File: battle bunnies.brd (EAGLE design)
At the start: 151.7 x 94 mm, 59 parts, among them IC1 CP2104, Q1 mmbt2222, Q2 mmbt2222, SW2 KMR2, U1 PCA9685, U2 SPX3819, U3 MCP73831T-2ACI/OT, X2 ESP-12, X4 20329

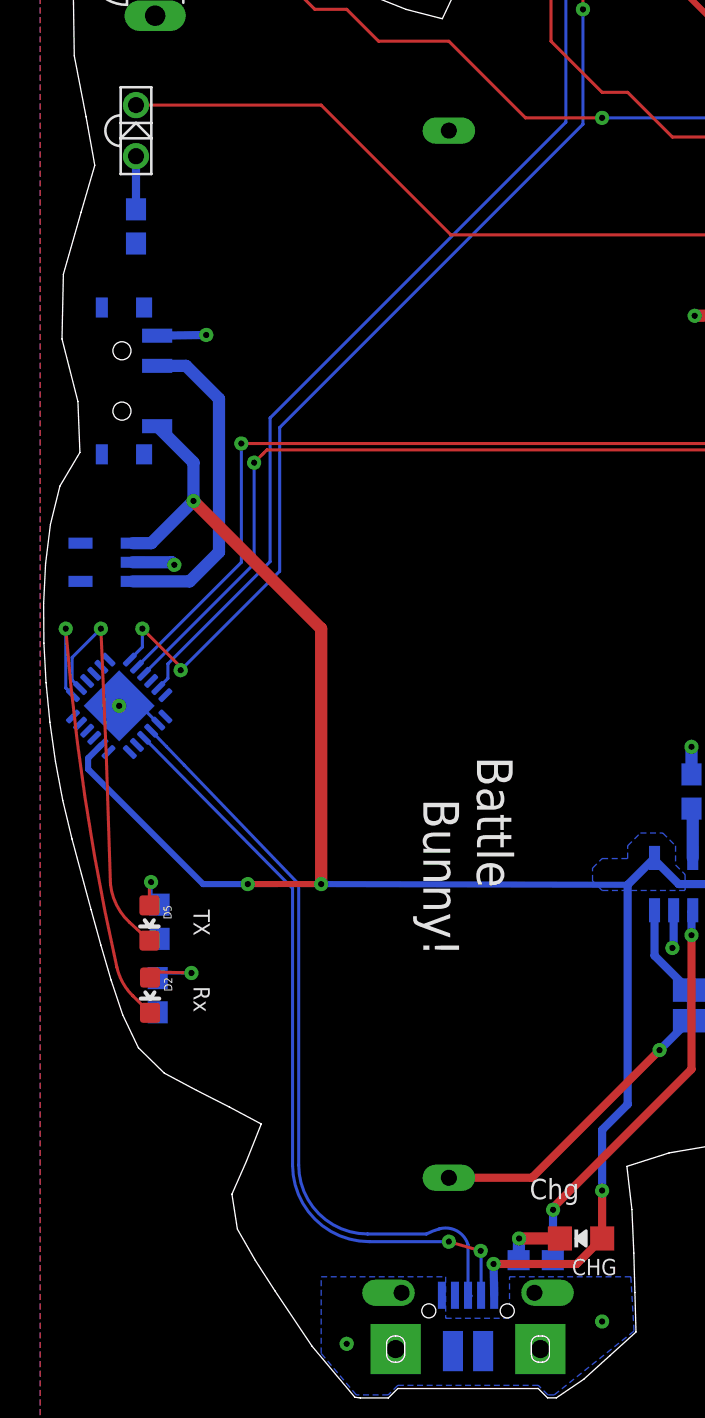
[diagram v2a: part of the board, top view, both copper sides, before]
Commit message: Fixing the USB impedance issue (moving USB chip)
This is a pretty big change as I'm moving a bunch of stuff around
which obviously causes it's own issues, but this should be ok
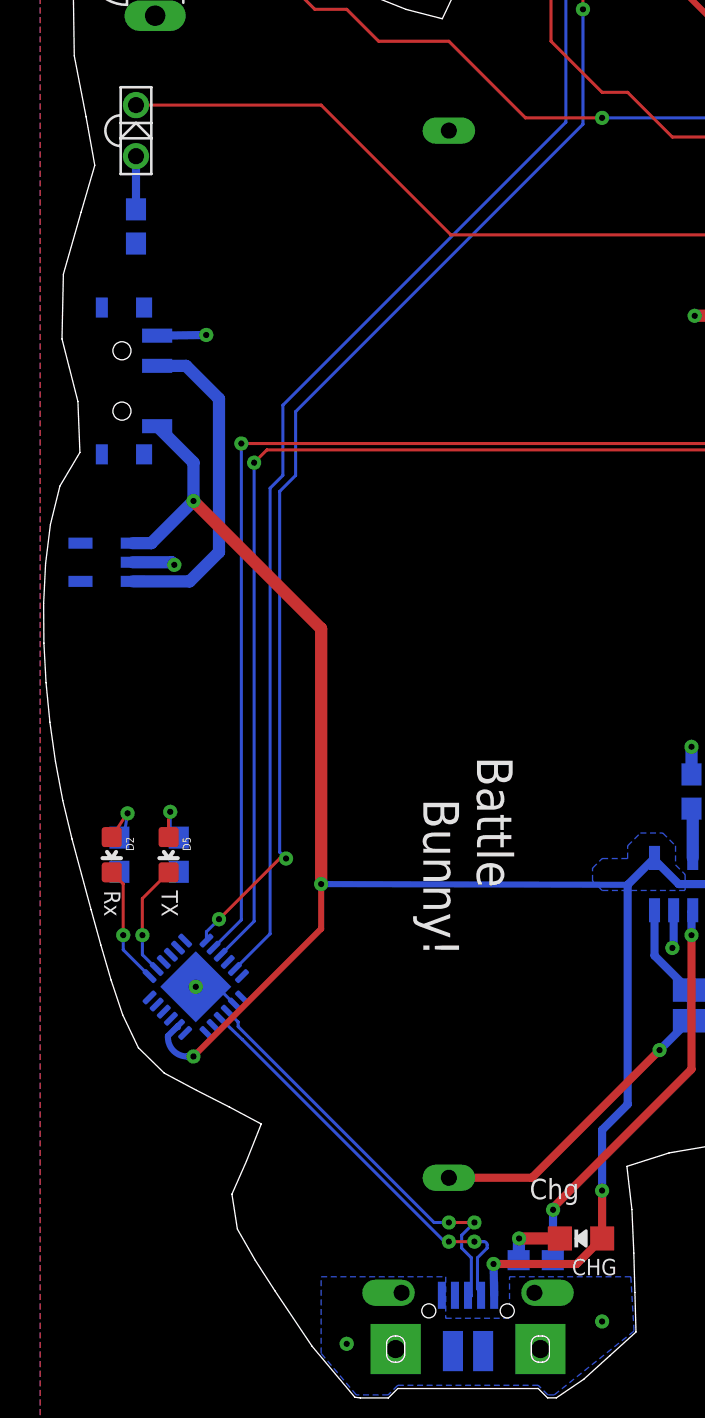
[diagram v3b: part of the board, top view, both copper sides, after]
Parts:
- moved IC1 14.5 mm to (7.74, 21.6)
- moved D2 7.24 mm to (3.56, 28.1)
- moved R15 7.24 mm to (3.94, 28.1)
- moved D5 3.53 mm to (6.38, 28.1)
- moved R1 3.47 mm to (6.89, 28.1)
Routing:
- net RXLED: track 23.3 -> 5.94 mm
- net USBD_N: track 37.5 -> 20.6 mm
- net USBD_P: track 37.3 -> 21.0 mm, vias 0 -> 2
- net TXLED: track 19.9 -> 5.64 mm
- net DTR: track 49.3 -> 61.7 mm
- net USB_RX: track 51.0 -> 63.4 mm
- net TXD: track 177.3 -> 189.7 mm
- net RTS: track 52.7 -> 61.5 mm
- net VBUS: track 98.2 -> 96.4 mm
- net N$10: track 3.96 -> 2.74 mm

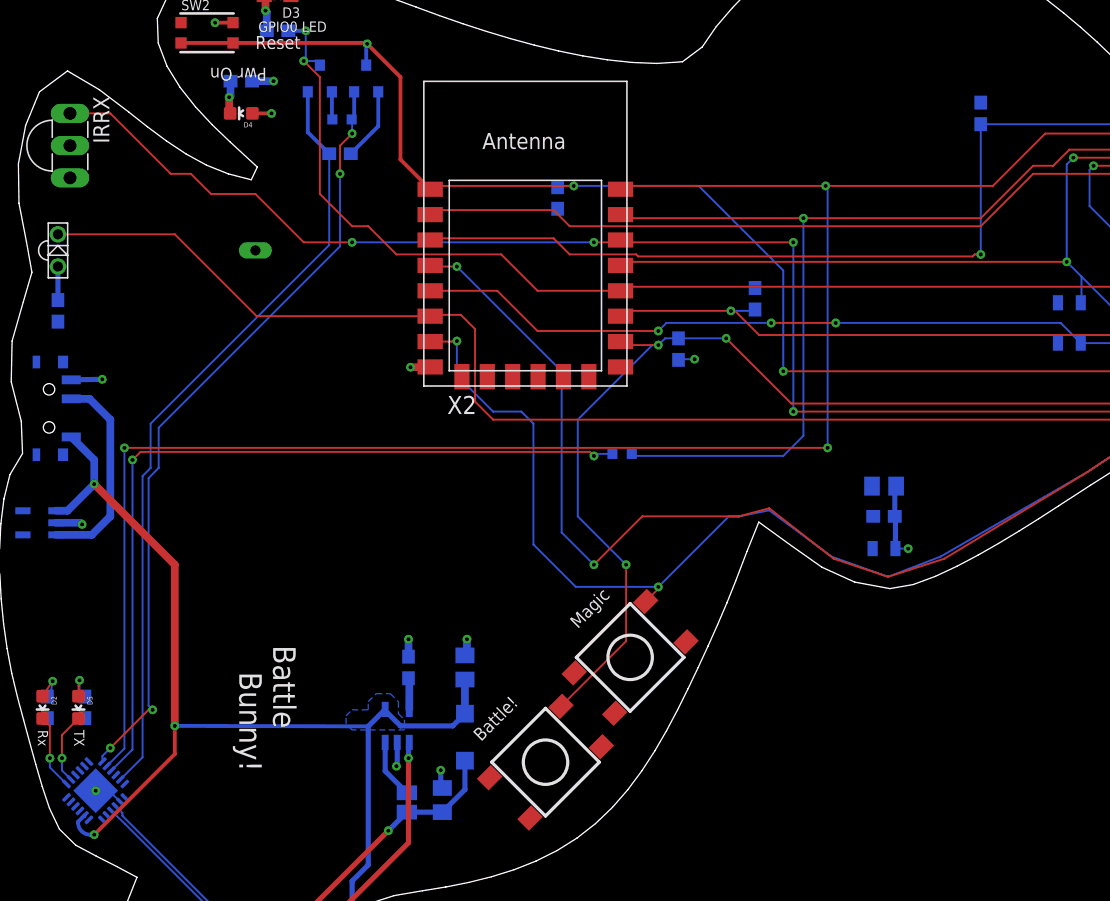
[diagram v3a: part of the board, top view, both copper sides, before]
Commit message: Adding some clearances around lines passing through the ESP8266
This *SHOULDN'T* be the problem with the IR RX but it can't hurt
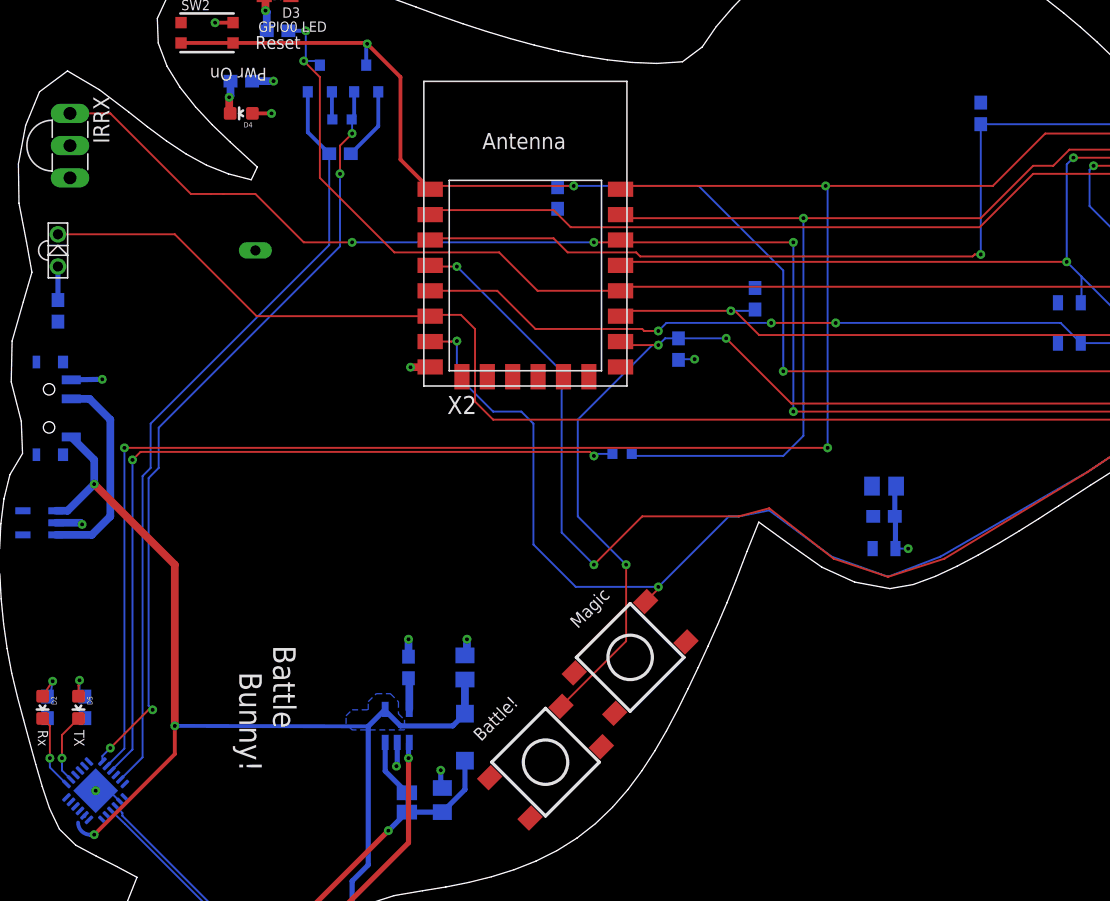
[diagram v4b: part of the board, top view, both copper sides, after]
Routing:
- net VBUS: track 96.4 -> 95.7 mm
- net GPIO0: track 147.4 -> 146.6 mm
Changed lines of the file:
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@@
 <wire x1="6.35" y1="19.05" x2="7.3025" y2="18.0975" width="0.3048" layer="16" curve="90"/>
 <wire x1="7.3025" y1="18.0975" x2="7.62" y2="18.0975" width="0.3048" layer="16"/>
-<wire x1="6.35" y1="19.05" x2="6.35" y2="19.117696875" width="0.3048" layer="16"/>
-<wire x1="6.35" y1="19.117696875" x2="6.8518375" y2="19.619534375" width="0.3048" layer="16"/>
+<wire x1="6.35" y1="19.05" x2="6.8518375" y2="19.5518375" width="0" layer="19" extent="16-16"/>
 </signal>
 <signal name="VBAT">
@@
 <contactref element="JP4" pad="5"/>
 <wire x1="135.5725" y1="87.3125" x2="135.5725" y2="85.725" width="0.1524" layer="1"/>
-<wire x1="81.5975" y1="70.1675" x2="77.47" y2="66.04" width="0.1524" layer="1"/>
-<wire x1="77.47" y1="66.04" x2="45.085" y2="66.04" width="0.1524" layer="1"/>
-<wire x1="45.085" y1="66.04" x2="43.815" y2="67.31" width="0.1524" layer="1"/>
+<wire x1="81.5975" y1="70.1675" x2="77.390625" y2="65.960625" width="0.1524" layer="1"/>
 <wire x1="43.815" y1="67.31" x2="34.45" y2="67.31" width="0.1524" layer="1"/>
 <wire x1="34.45" y1="67.31" x2="34.0925" y2="66.9525" width="0.1524" layer="1"/>
@@
 <wire x1="106.9975" y1="70.1675" x2="81.5975" y2="70.1675" width="0.1524" layer="1"/>
 <wire x1="107.95" y1="71.12" x2="106.9975" y2="70.1675" width="0.1524" layer="1"/>
+<wire x1="43.815" y1="67.31" x2="45.164375" y2="65.960625" width="0.1524" layer="1"/>
+<wire x1="45.164375" y1="65.960625" x2="77.390625" y2="65.960625" width="0.1524" layer="1"/>
 </signal>
 <signal name="CH_PD">
@@
 <contactref element="R3" pad="1"/>
 <contactref element="JP4" pad="10"/>
-<wire x1="45.085" y1="63.8175" x2="43.815" y2="65.0875" width="0.1524" layer="1"/>
 <wire x1="43.815" y1="65.0875" x2="34.2275" y2="65.0875" width="0.1524" layer="1"/>
 <wire x1="34.2275" y1="65.0875" x2="34.0925" y2="64.9525" width="0.1524" layer="1"/>
-<wire x1="45.085" y1="63.8175" x2="50.32375" y2="63.8175" width="0.1524" layer="1"/>
-<wire x1="50.32375" y1="63.8175" x2="50.4825" y2="63.65875" width="0.1524" layer="1"/>
-<wire x1="50.4825" y1="63.65875" x2="76.835" y2="63.65875" width="0.1524" layer="1"/>
+<wire x1="50.64125" y1="63.65875" x2="76.835" y2="63.65875" width="0.1524" layer="1"/>
 <wire x1="76.835" y1="63.65875" x2="76.99375" y2="63.8175" width="0.1524" layer="1"/>
 <wire x1="76.99375" y1="63.8175" x2="77.47" y2="63.8175" width="0.1524" layer="1"/>
@@
 <wire x1="121.76125" y1="80.16875" x2="122.8725" y2="81.28" width="0.1524" layer="16"/>
 <wire x1="122.8725" y1="81.28" x2="122.8725" y2="87.3125" width="0.1524" layer="16"/>
+<wire x1="43.815" y1="65.0875" x2="44.92625" y2="63.97625" width="0.1524" layer="1"/>
+<wire x1="44.92625" y1="63.97625" x2="50.32375" y2="63.97625" width="0.1524" layer="1"/>
+<wire x1="50.32375" y1="63.97625" x2="50.64125" y2="63.65875" width="0.1524" layer="1"/>
 </signal>
 <signal name="GPIO16">
@@
 <contactref element="JP2" pad="3"/>
 <wire x1="49.0925" y1="60.9525" x2="42.5525" y2="60.9525" width="0.1524" layer="1"/>
-<wire x1="42.5525" y1="60.9525" x2="39.6875" y2="63.8175" width="0.1524" layer="1"/>
-<wire x1="39.6875" y1="63.8175" x2="31.4325" y2="63.8175" width="0.1524" layer="1"/>
-<wire x1="31.4325" y1="63.8175" x2="29.21" y2="66.04" width="0.1524" layer="1"/>
-<wire x1="29.21" y1="66.04" x2="27.94" y2="66.04" width="0.1524" layer="1"/>
-<wire x1="27.94" y1="66.04" x2="25.4" y2="68.58" width="0.1524" layer="1"/>
-<wire x1="25.4" y1="68.58" x2="25.4" y2="77.7875" width="0.1524" layer="1"/>
+<wire x1="42.5525" y1="60.9525" x2="39.52875" y2="63.97625" width="0.1524" layer="1"/>
+<wire x1="25.4" y1="69.85" x2="25.4" y2="77.7875" width="0.1524" layer="1"/>
 <wire x1="25.4" y1="77.7875" x2="24.13" y2="79.0575" width="0.1524" layer="1"/>
 <via x="24.13" y="79.0575" extent="1-16" drill="0.3048" diameter="0.3048"/>
@@
 <wire x1="24.28875" y1="81.43875" x2="24.28875" y2="79.21625" width="0.1524" layer="16"/>
 <wire x1="24.28875" y1="79.21625" x2="24.13" y2="79.0575" width="0.1524" layer="16"/>
+<wire x1="39.52875" y1="63.97625" x2="31.27375" y2="63.97625" width="0.1524" layer="1"/>
+<wire x1="31.27375" y1="63.97625" x2="25.4" y2="69.85" width="0.1524" layer="1"/>
 </signal>
 <signal name="RXD">
@@
 <via x="62.70625" y="51.435" extent="1-16" drill="0.3048"/>
 <wire x1="8.89" y1="74.93" x2="5.715" y2="74.93" width="0.1524" layer="1"/>
-<wire x1="16.8275" y1="68.58" x2="15.24" y2="70.1675" width="0.1524" layer="1"/>
-<wire x1="13.6525" y1="70.1675" x2="8.89" y2="74.93" width="0.1524" layer="1"/>
-<wire x1="16.8275" y1="68.58" x2="20.32" y2="68.58" width="0.1524" layer="1"/>
+<wire x1="15.24" y1="68.58" x2="8.89" y2="74.93" width="0.1524" layer="1"/>
+<wire x1="16.8275" y1="68.58" x2="17.78" y2="68.58" width="0.1524" layer="1"/>
+<wire x1="17.78" y1="68.58" x2="20.32" y2="68.58" width="0.1524" layer="1"/>
 <wire x1="20.32" y1="68.58" x2="24.13" y2="64.77" width="0.1524" layer="1"/>
 <wire x1="49.0925" y1="64.9525" x2="48.91" y2="64.77" width="0.1524" layer="1"/>
@@
 <wire x1="120.65" y1="48.26" x2="121.92" y2="46.99" width="0.1524" layer="16"/>
 <wire x1="121.92" y1="46.99" x2="121.92" y2="41.91" width="0.1524" layer="16"/>
-<wire x1="15.24" y1="70.1675" x2="13.6525" y2="70.1675" width="0.1524" layer="1"/>
+<wire x1="15.24" y1="68.58" x2="16.8275" y2="68.58" width="0.1524" layer="1"/>
 </signal>
 <signal name="GPIO4/SDA">
@@
 <wire x1="133.0325" y1="84.1375" x2="133.0325" y2="87.3125" width="0.1524" layer="1"/>
 <wire x1="88.5825" y1="56.8325" x2="85.355" y2="56.8325" width="0.1524" layer="16"/>
-<wire x1="42.545" y1="57.785" x2="39.3775" y2="60.9525" width="0.1524" layer="1"/>
 <wire x1="39.3775" y1="60.9525" x2="34.0925" y2="60.9525" width="0.1524" layer="1"/>
-<wire x1="42.545" y1="57.785" x2="52.07" y2="57.785" width="0.1524" layer="1"/>
 <wire x1="133.0325" y1="84.1375" x2="130.175" y2="81.28" width="0.1524" layer="1"/>
 <wire x1="130.175" y1="81.28" x2="128.27" y2="81.28" width="0.1524" layer="1"/>
@@
 <wire x1="88.5825" y1="56.8325" x2="91.055" y2="59.305" width="0.1524" layer="16"/>
 <wire x1="91.055" y1="59.305" x2="91.055" y2="60.5822" width="0.1524" layer="16"/>
+<wire x1="39.3775" y1="60.9525" x2="42.38625" y2="57.94375" width="0.1524" layer="1"/>
+<wire x1="42.38625" y1="57.94375" x2="50.8" y2="57.94375" width="0.1524" layer="1"/>
+<wire x1="50.8" y1="57.94375" x2="50.95875" y2="57.785" width="0.1524" layer="1"/>
+<wire x1="50.95875" y1="57.785" x2="52.07" y2="57.785" width="0.1524" layer="1"/>
 </signal>
 <signal name="GPIO13/MOSI">

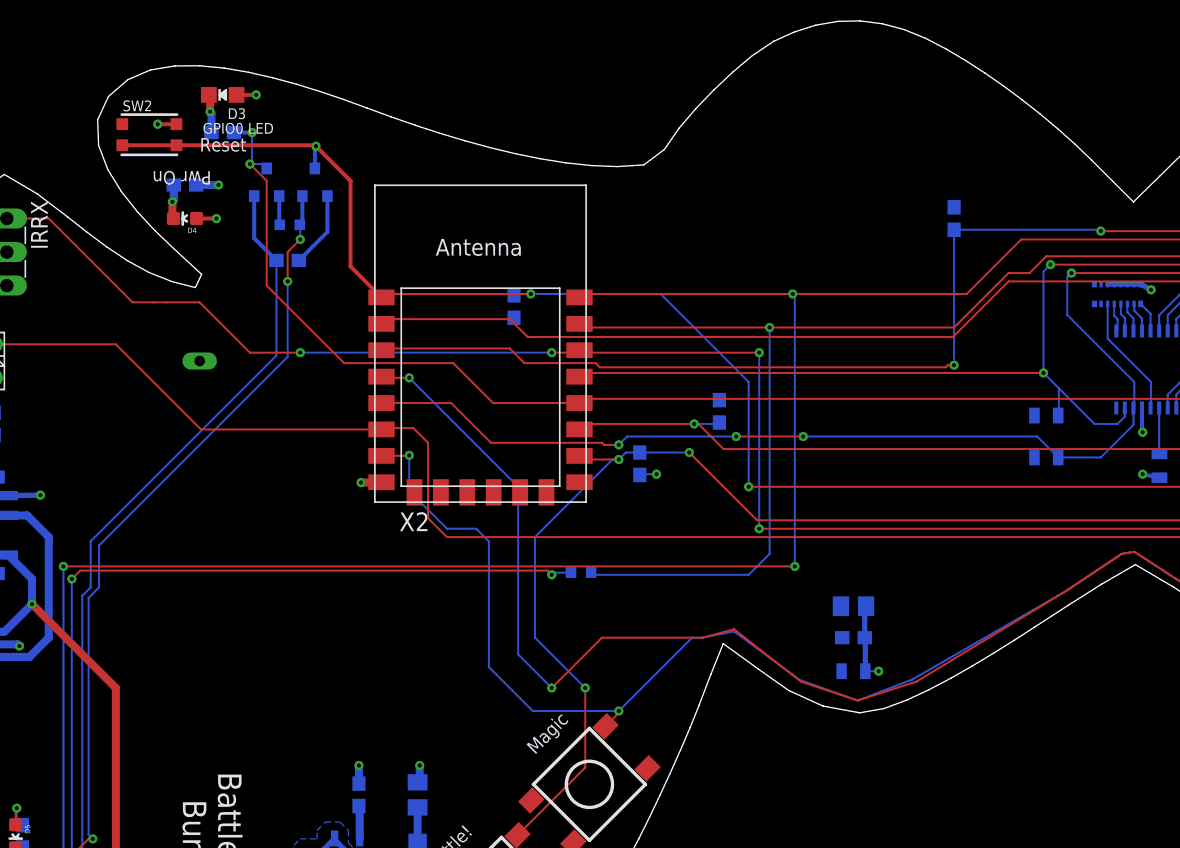
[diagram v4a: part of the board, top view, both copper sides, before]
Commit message: Cleaning up various DRC errors (mostly stop mask issues)
This should also make the general text easier to read
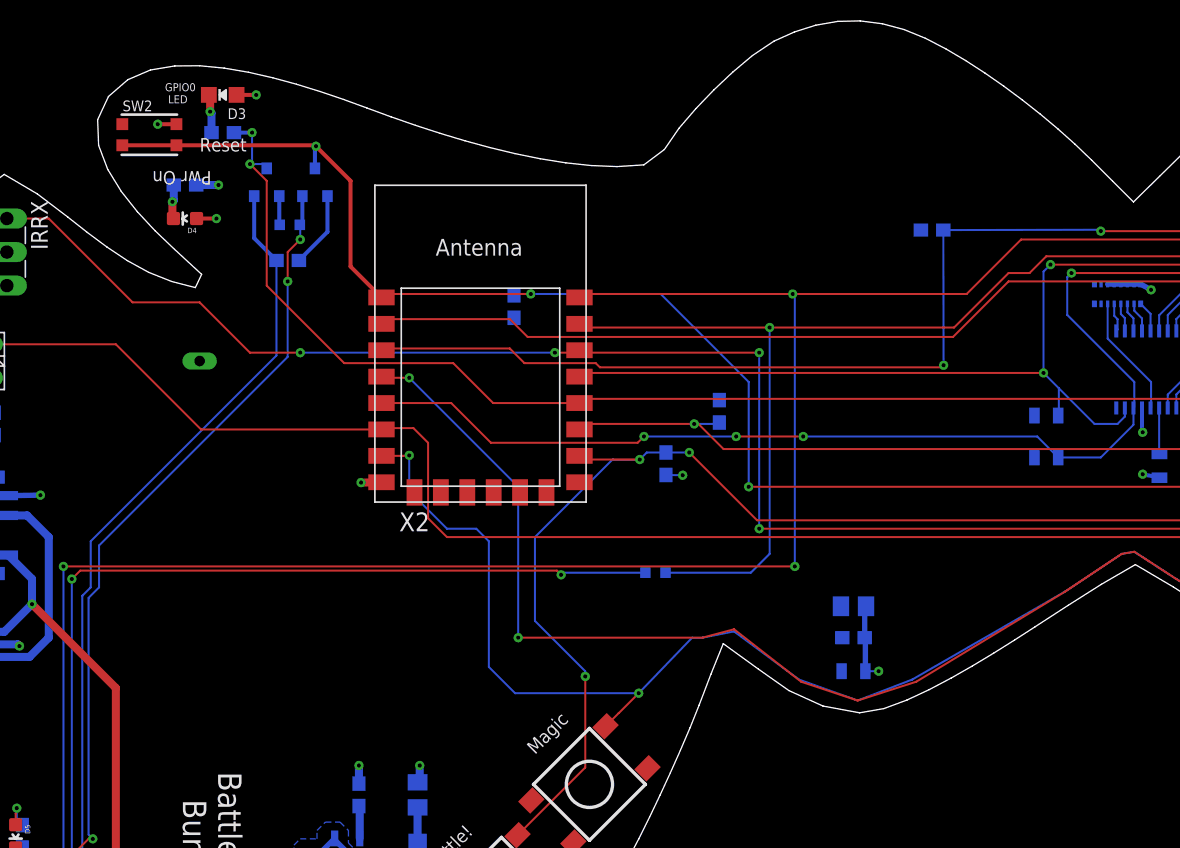
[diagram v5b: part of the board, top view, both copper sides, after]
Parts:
- moved R12 5.64 mm to (54.8, 48.1)
- moved R6 1.98 mm to (55.6, 56.4)
- moved R3 1.88 mm to (75.8, 74.1), turned to 0 degrees
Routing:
- net RXD: track 122.6 -> 116.8 mm
- net USB_RX: track 63.4 -> 69.1 mm
- net GPIO16: track 123.7 -> 119.8 mm
- net GPIO15: track 126.6 -> 128.2 mm
- net GPIO13/MOSI: track 131.2 -> 132.1 mm
